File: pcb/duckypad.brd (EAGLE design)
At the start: 110 x 96 mm, 161 parts, among them IC2 REG1117, SW1 SPST_TACT-EVQQ2, SW2 SPST_TACT-EVQQ2, SW21 EC12E_SW, SW22 EC12E_SW, SW3 324_SW324_SWITCH_FOOT_HOLE, SW4 324_SW324_SWITCH_FOOT_HOLE, U1 USBC_16P, U2 USBC_16P, U3 ESP32-S3FN8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

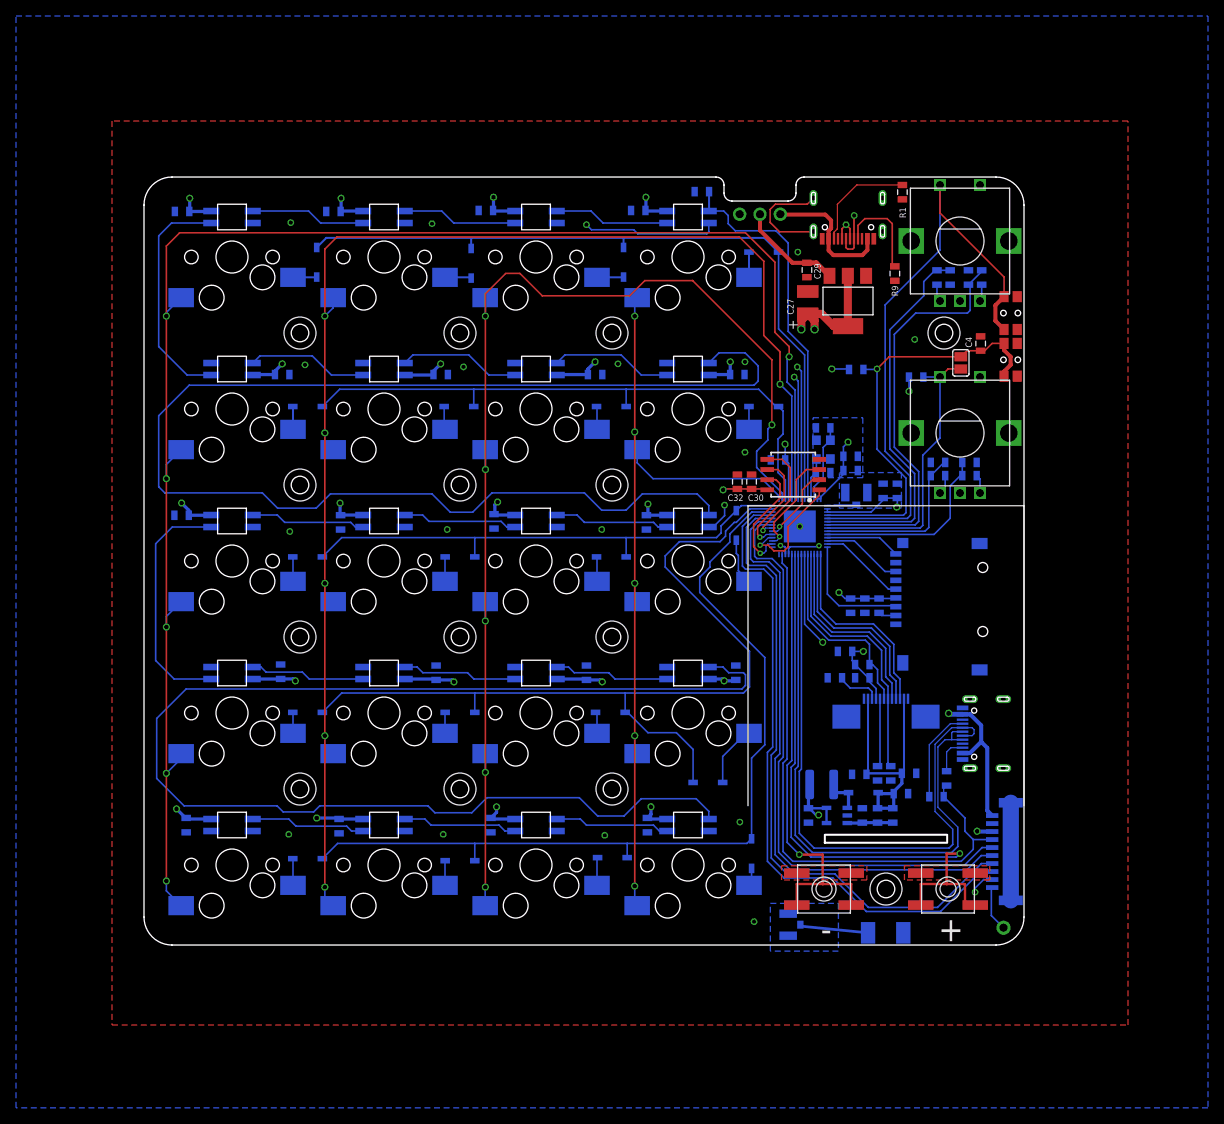
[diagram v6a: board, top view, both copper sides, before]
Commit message: wired up CC pins
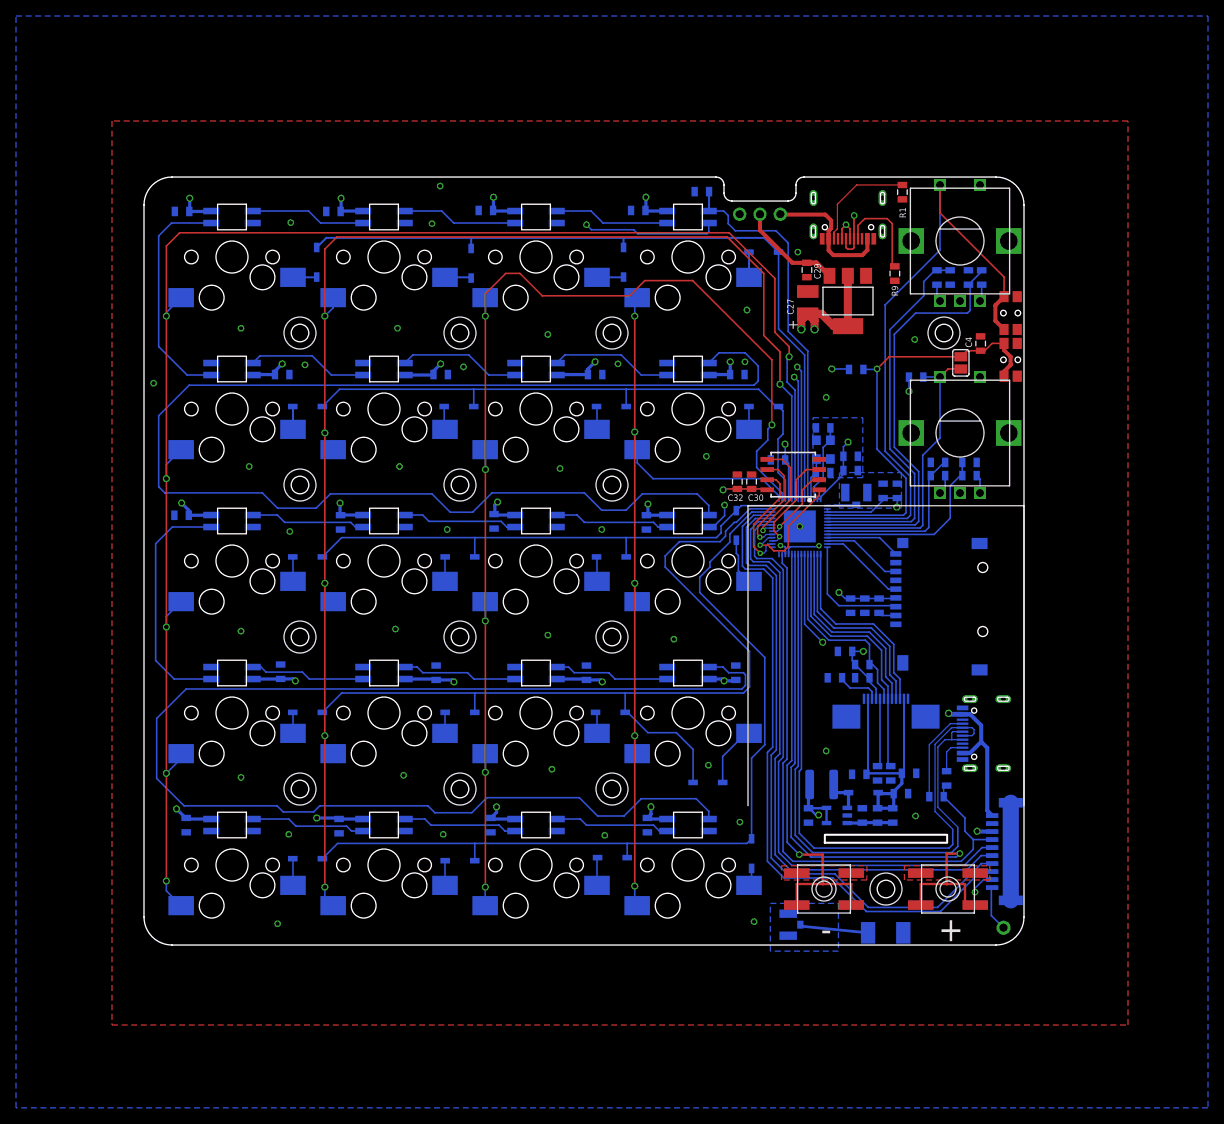
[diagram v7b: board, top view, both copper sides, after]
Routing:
- net GND: track 46.6 -> 33.1 mm, vias 20 -> 41
- net COL0: track 207.0 -> 205.8 mm
- net COL1: track 181.1 -> 180.2 mm
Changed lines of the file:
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@@
 <layer number="20" name="Dimension" color="15" fill="1" visible="yes" active="yes"/>
 <layer number="21" name="tPlace" color="7" fill="1" visible="yes" active="yes"/>
-<layer number="22" name="bPlace" color="7" fill="1" visible="yes" active="yes"/>
+<layer number="22" name="bPlace" color="7" fill="1" visible="no" active="yes"/>
 <layer number="23" name="tOrigins" color="15" fill="1" visible="yes" active="yes"/>
-<layer number="24" name="bOrigins" color="15" fill="1" visible="yes" active="yes"/>
+<layer number="24" name="bOrigins" color="15" fill="1" visible="no" active="yes"/>
 <layer number="25" name="tNames" color="7" fill="1" visible="yes" active="yes"/>
-<layer number="26" name="bNames" color="7" fill="1" visible="yes" active="yes"/>
-<layer number="27" name="tValues" color="7" fill="1" visible="yes" active="yes"/>
-<layer number="28" name="bValues" color="7" fill="1" visible="yes" active="yes"/>
+<layer number="26" name="bNames" color="7" fill="1" visible="no" active="yes"/>
+<layer number="27" name="tValues" color="7" fill="1" visible="no" active="yes"/>
+<layer number="28" name="bValues" color="7" fill="1" visible="no" active="yes"/>
 <layer number="29" name="tStop" color="7" fill="3" visible="no" active="yes"/>
 <layer number="30" name="bStop" color="7" fill="6" visible="no" active="yes"/>
@@
 <layer number="38" name="bTest" color="7" fill="1" visible="no" active="yes"/>
 <layer number="39" name="tKeepout" color="4" fill="11" visible="yes" active="yes"/>
-<layer number="40" name="bKeepout" color="1" fill="11" visible="yes" active="yes"/>
+<layer number="40" name="bKeepout" color="1" fill="11" visible="no" active="yes"/>
 <layer number="41" name="tRestrict" color="4" fill="10" visible="yes" active="yes"/>
-<layer number="42" name="bRestrict" color="1" fill="10" visible="yes" active="yes"/>
+<layer number="42" name="bRestrict" color="1" fill="10" visible="no" active="yes"/>
 <layer number="43" name="vRestrict" color="2" fill="10" visible="no" active="yes"/>
 <layer number="44" name="Drills" color="7" fill="1" visible="yes" active="yes"/>
@@
 <layer number="50" name="dxf" color="7" fill="1" visible="no" active="no"/>
 <layer number="51" name="tDocu" color="7" fill="1" visible="yes" active="yes"/>
-<layer number="52" name="bDocu" color="7" fill="1" visible="yes" active="yes"/>
+<layer number="52" name="bDocu" color="7" fill="1" visible="no" active="yes"/>
 <layer number="53" name="tGND_GNDA" color="7" fill="9" visible="no" active="no"/>
 <layer number="54" name="bGND_GNDA" color="1" fill="9" visible="no" active="no"/>
@@
 <rectangle x1="81.534" y1="-2.286" x2="113.792" y2="7.62" layer="41"/>
 <rectangle x1="81.28" y1="-2.286" x2="113.538" y2="7.62" layer="42"/>
+<rectangle x1="75.184" y1="89.662" x2="80.772" y2="92.964" layer="41"/>
+<rectangle x1="75.438" y1="89.662" x2="81.026" y2="92.964" layer="42"/>
 </plain>
 <attributes>
@@
 <via x="81.722" y="86.614" extent="1-16" drill="0.5"/>
 <wire x1="83.68" y1="89.1945" x2="83.6395" y2="89.154" width="0.2032" layer="1"/>
-<wire x1="82.9139" y1="92.6084" x2="83.68" y2="93.3745" width="0.2032" layer="1"/>
-<wire x1="83.6395" y1="89.154" x2="79.436" y2="89.154" width="0.2032" layer="1"/>
-<wire x1="78.2676" y1="90.3224" x2="78.2676" y2="91.948" width="0.2032" layer="1"/>
-<wire x1="78.2676" y1="91.948" x2="78.928" y2="92.6084" width="0.2032" layer="1"/>
-<wire x1="79.436" y1="89.154" x2="78.2676" y2="90.3224" width="0.2032" layer="1"/>
-<wire x1="78.928" y1="92.6084" x2="82.9139" y2="92.6084" width="0.2032" layer="1"/>
 <contactref element="C46" pad="1"/>
 <contactref element="R17" pad="1"/>
@@
 <contactref element="SW4" pad="P$4"/>
 <contactref element="SW4" pad="P$1"/>
-<via x="75.118" y="61.595" extent="1-16" drill="0.5"/>
+<via x="70.292" y="61.087" extent="1-16" drill="0.5"/>
 <contactref element="SW1" pad="A"/>
 <contactref element="SW1" pad="A'"/>
@@
 <contactref element="U$3" pad="FIT@1"/>
 <wire x1="108.35" y1="5.584" x2="108.35" y2="17.784" width="2.032" layer="16"/>
+<via x="37.018" y="94.869" extent="1-16" drill="0.5"/>
+<via x="12.126" y="77.089" extent="1-16" drill="0.5"/>
+<via x="31.684" y="77.089" extent="1-16" drill="0.5"/>
+<via x="50.48" y="76.327" extent="1-16" drill="0.5"/>
+<via x="75.372" y="79.375" extent="1-16" drill="0.5"/>
+<via x="52.004" y="59.563" extent="1-16" drill="0.5"/>
+<via x="31.938" y="59.817" extent="1-16" drill="0.5"/>
+<via x="13.142" y="59.817" extent="1-16" drill="0.5"/>
+<via x="1.204" y="70.231" extent="1-16" drill="0.5"/>
+<via x="31.43" y="39.497" extent="1-16" drill="0.5"/>
+<via x="12.126" y="39.243" extent="1-16" drill="0.5"/>
+<via x="50.48" y="38.735" extent="1-16" drill="0.5"/>
+<via x="66.228" y="38.227" extent="1-16" drill="0.5"/>
+<via x="70.546" y="22.479" extent="1-16" drill="0.5"/>
+<via x="50.988" y="21.971" extent="1-16" drill="0.5"/>
+<via x="32.446" y="21.209" extent="1-16" drill="0.5"/>
+<via x="12.126" y="20.955" extent="1-16" drill="0.5"/>
+<via x="16.698" y="2.667" extent="1-16" drill="0.5"/>
+<via x="96.454" y="16.129" extent="1-16" drill="0.5"/>
+<via x="85.278" y="24.257" extent="1-16" drill="0.5"/>
+<via x="85.278" y="68.453" extent="1-16" drill="0.5"/>
 </signal>
 <signal name="+3V3">
@@
 <wire x1="4.445" y1="89.027" x2="2.794" y2="87.376" width="0.2032" layer="1"/>
 <wire x1="2.794" y1="78.613" x2="2.794" y2="87.376" width="0.2032" layer="1"/>
-<wire x1="4.445" y1="89.027" x2="75.184" y2="89.027" width="0.2032" layer="1"/>
-<wire x1="75.184" y1="89.027" x2="78.867" y2="85.344" width="0.2032" layer="1"/>
+<wire x1="4.445" y1="89.027" x2="73.152" y2="89.027" width="0.2032" layer="1"/>
+<wire x1="73.152" y1="89.027" x2="78.867" y2="83.312" width="0.2032" layer="1"/>
 <wire x1="80.645" y1="74.803" x2="78.867" y2="76.581" width="0.2032" layer="1"/>
 <wire x1="80.645" y1="74.803" x2="80.645" y2="73.533" width="0.2032" layer="1"/>
 <via x="80.645" y="73.533" extent="1-16" drill="0.55"/>
-<wire x1="78.867" y1="85.344" x2="78.867" y2="76.581" width="0.2032" layer="1"/>
+<wire x1="78.867" y1="83.312" x2="78.867" y2="76.581" width="0.2032" layer="1"/>
 <contactref element="U3" pad="48"/>
 <wire x1="80.645" y1="73.533" x2="80.391" y2="73.279" width="0.2032" layer="16"/>
@@
 <wire x1="24.13" y1="88.519" x2="22.606" y2="86.995" width="0.2032" layer="1"/>
 <wire x1="22.606" y1="78.613" x2="22.606" y2="86.995" width="0.2032" layer="1"/>
-<wire x1="74.422" y1="88.519" x2="77.47" y2="85.471" width="0.2032" layer="1"/>
-<wire x1="77.47" y1="85.471" x2="77.47" y2="76.2" width="0.2032" layer="1"/>
+<wire x1="72.898" y1="88.519" x2="77.47" y2="83.947" width="0.2032" layer="1"/>
+<wire x1="77.47" y1="83.947" x2="77.47" y2="76.2" width="0.2032" layer="1"/>
 <wire x1="79.502" y1="74.168" x2="79.502" y2="70.104" width="0.2032" layer="1"/>
 <via x="79.502" y="70.104" extent="1-16" drill="0.55"/>
-<wire x1="24.13" y1="88.519" x2="74.422" y2="88.519" width="0.2032" layer="1"/>
+<wire x1="24.13" y1="88.519" x2="72.898" y2="88.519" width="0.2032" layer="1"/>
 <wire x1="77.47" y1="76.2" x2="79.502" y2="74.168" width="0.2032" layer="1"/>
 <contactref element="U3" pad="47"/>

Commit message: adjusted component values
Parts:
- C1, C10, C2, C9: value 10nF -> 100nF
- C27: value 47uF -> 100uF
- C29: value 10uF -> 4.7uF
- C34, C38: value 2.2uF -> 4.7uF
- C35: value 22pF -> 12pF
- C4: value 1uF -> 100nF
- R13, R14, R15, R2, R8: value 10K -> 62K
- R5: value 5.1K -> 10K
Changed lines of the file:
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@@
 <attribute name="NAME" x="35.3416" y="36.3855" size="0.8128" layer="26" rot="MR180"/>
 </element>
-<element name="R5" library="clock" package="0805" value="5.1K" x="69.7334" y="94.1738" smashed="yes" rot="MR180">
+<element name="R5" library="clock" package="0805" value="10K" x="69.7334" y="94.1738" smashed="yes" rot="MR180">
 <attribute name="NAME" x="66.3806" y="94.6945" size="0.8128" layer="26" rot="MR180"/>
 </element>
-<element name="C27" library="clock" package="C1210" value="47uF" x="82.971" y="80.297" smashed="yes" rot="R90">
+<element name="C27" library="clock" package="C1210" value="100uF" x="82.971" y="80.297" smashed="yes" rot="R90">
 <attribute name="NAME" x="80.3936" y="80.7764" size="0.8128" layer="25" rot="R270"/>
 </element>
@@
 <attribute name="NAME" x="93.4593" y="82.4334" size="0.8128" layer="25" rot="R270"/>
 </element>
-<element name="C29" library="clock" package="0805" value="10uF" x="82.87" y="84.3788" smashed="yes" rot="R90">
+<element name="C29" library="clock" package="0805" value="4.7uF" x="82.87" y="84.3788" smashed="yes" rot="R90">
 <attribute name="NAME" x="84.5845" y="83.2358" size="0.8128" layer="25" rot="R90"/>
 </element>
@@
 <attribute name="PROD_ID" value="XTAL-12454" x="85.9224" y="66.9252" size="1.778" layer="28" rot="MR270" display="off"/>
 </element>
-<element name="R2" library="joyAnalog" package="0805" value="10K" x="89.027" y="71.948" smashed="yes" rot="MR180">
+<element name="R2" library="joyAnalog" package="0805" value="62K" x="89.027" y="71.948" smashed="yes" rot="MR180">
 <attribute name="NAME" x="86.106" y="72.3925" size="0.8128" layer="26" rot="MR180"/>
 </element>
-<element name="C4" library="clock" package="0805" value="1uF" x="104.582" y="75.184" smashed="yes" rot="R90">
+<element name="C4" library="clock" package="0805" value="100nF" x="104.582" y="75.184" smashed="yes" rot="R90">
 <attribute name="NAME" x="103.5025" y="74.676" size="0.8128" layer="25" rot="R90"/>
 </element>
@@
 <attribute name="NAME" x="82.103" y="15.0495" size="0.8128" layer="26" rot="MR0"/>
 </element>
-<element name="C35" library="clock" package="0805" value="22pF" x="91.694" y="16.195" smashed="yes" rot="MR90">
+<element name="C35" library="clock" package="0805" value="12pF" x="91.694" y="16.195" smashed="yes" rot="MR90">
 <attribute name="NAME" x="90.993" y="14.7955" size="0.8128" layer="26" rot="MR180"/>
 </element>
@@
 <attribute name="NAME" x="96.393" y="22.2885" size="0.8128" layer="26" rot="MR0"/>
 </element>
-<element name="C34" library="clock" package="0805" value="2.2uF" x="86.36" y="33.401" smashed="yes" rot="MR180">
+<element name="C34" library="clock" package="0805" value="4.7uF" x="86.36" y="33.401" smashed="yes" rot="MR180">
 <attribute name="NAME" x="84.836" y="32.9565" size="0.8128" layer="26" rot="MR0"/>
 </element>
@@
 <attribute name="NAME" x="91.5645" y="44.196" size="0.8128" layer="26" rot="MR90"/>
 </element>
-<element name="C38" library="clock" package="0805" value="2.2uF" x="88.326" y="42.418" smashed="yes" rot="MR90">
+<element name="C38" library="clock" package="0805" value="4.7uF" x="88.326" y="42.418" smashed="yes" rot="MR90">
 <attribute name="NAME" x="88.0085" y="44.196" size="0.8128" layer="26" rot="MR90"/>
 </element>
@@
 <attribute name="NAME" x="4.125" y="13.6525" size="0.8128" layer="26" rot="MR0"/>
 </element>
-<element name="C1" library="clock" package="0805" value="10nF" x="100.772" y="83.439" smashed="yes" rot="MR90">
+<element name="C1" library="clock" package="0805" value="100nF" x="100.772" y="83.439" smashed="yes" rot="MR90">
 <attribute name="NAME" x="100.4545" y="84.963" size="0.8128" layer="26" rot="MR90"/>
 </element>
-<element name="R8" library="joyAnalog" package="0805" value="10K" x="99.121" y="83.439" smashed="yes" rot="MR270">
+<element name="R8" library="joyAnalog" package="0805" value="62K" x="99.121" y="83.439" smashed="yes" rot="MR270">
 <attribute name="NAME" x="98.6765" y="84.963" size="0.8128" layer="26" rot="MR90"/>
 </element>
-<element name="R13" library="joyAnalog" package="0805" value="10K" x="104.709" y="83.439" smashed="yes" rot="MR270">
+<element name="R13" library="joyAnalog" package="0805" value="62K" x="104.709" y="83.439" smashed="yes" rot="MR270">
 <attribute name="NAME" x="104.3915" y="84.963" size="0.8128" layer="26" rot="MR90"/>
 </element>
-<element name="C2" library="clock" package="0805" value="10nF" x="103.058" y="83.439" smashed="yes" rot="MR270">
+<element name="C2" library="clock" package="0805" value="100nF" x="103.058" y="83.439" smashed="yes" rot="MR270">
 <attribute name="NAME" x="102.7405" y="84.963" size="0.8128" layer="26" rot="MR90"/>
 </element>
-<element name="R14" library="joyAnalog" package="0805" value="10K" x="99.248" y="58.674" smashed="yes" rot="MR180">
+<element name="R14" library="joyAnalog" package="0805" value="62K" x="99.248" y="58.674" smashed="yes" rot="MR180">
 <attribute name="NAME" x="97.597" y="58.3565" size="0.8128" layer="26" rot="MR0"/>
 </element>
-<element name="C9" library="clock" package="0805" value="10nF" x="99.248" y="60.325" smashed="yes" rot="MR180">
+<element name="C9" library="clock" package="0805" value="100nF" x="99.248" y="60.325" smashed="yes" rot="MR180">
 <attribute name="NAME" x="97.597" y="59.8805" size="0.8128" layer="26" rot="MR0"/>
 </element>
-<element name="R15" library="joyAnalog" package="0805" value="10K" x="103.185" y="58.674" smashed="yes" rot="MR180">
+<element name="R15" library="joyAnalog" package="0805" value="62K" x="103.185" y="58.674" smashed="yes" rot="MR180">
 <attribute name="NAME" x="104.709" y="58.9915" size="0.8128" layer="26" rot="MR180"/>
 </element>
-<element name="C10" library="clock" package="0805" value="10nF" x="103.185" y="60.325" smashed="yes" rot="MR0">
+<element name="C10" library="clock" package="0805" value="100nF" x="103.185" y="60.325" smashed="yes" rot="MR0">
 <attribute name="NAME" x="104.709" y="60.6425" size="0.8128" layer="26" rot="MR180"/>
 </element>
